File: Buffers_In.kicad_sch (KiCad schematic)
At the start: 31 parts, among them U4 NE5532, U5 NE5532, X1 PEDAL_COMBO_TOP

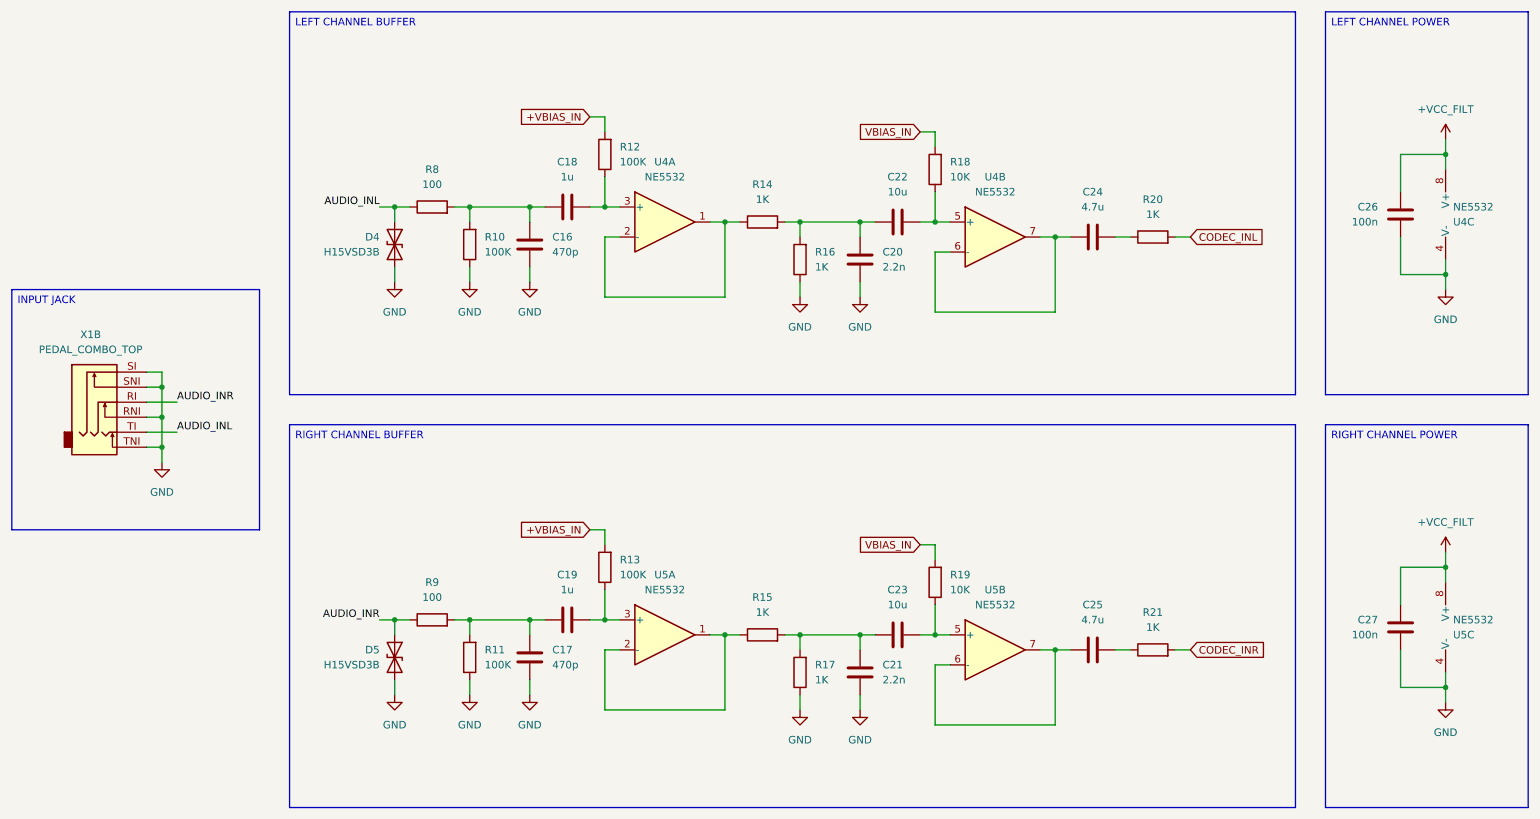
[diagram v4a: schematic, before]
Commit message: RP2350 layout
Updated the layout for the RP2350.
Added board headers.
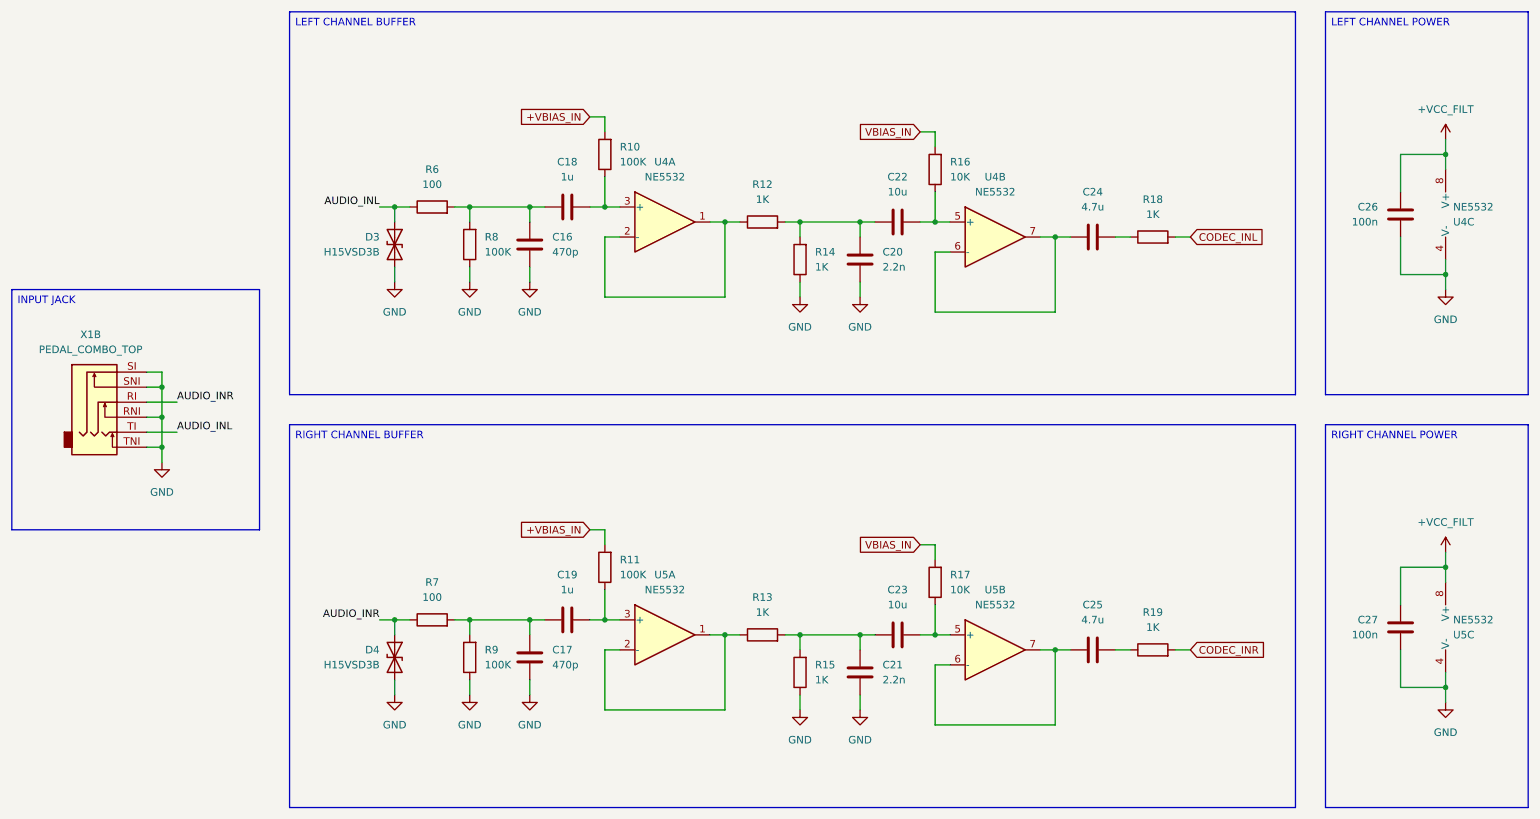
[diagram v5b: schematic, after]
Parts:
- renumbered D4 to D3, D5 to D4, R12 to R10, R13 to R11, R14 to R12, R15 to R13, R16 to R14, R17 to R15, R18 to R16, R19 to R17, R20 to R18, R21 to R19, R8 to R6, R9 to R7, R10 to R8, R11 to R9
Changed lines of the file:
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@@
 		(dnp no)
 		(fields_autoplaced yes)
-		(property "Reference" "R9"
+		(property "Reference" "R7"
 			(at 90.17 118.11 90)
 			(effects
@@
 			(project "SimpleCodec"
 				(path "/4cbf131b-42e8-4a05-beea-68c6d66cdb1a/469e8ad1-854f-4ea5-8b66-be90c8cb100f"
-					(reference "R9")
+					(reference "R7")
 					(unit 1)
 				)
@@
 		(dnp no)
 		(fields_autoplaced yes)
-		(property "Reference" "R19"
+		(property "Reference" "R17"
 			(at 177.8 116.8399 0)
 			(effects
@@
 			(project "SimpleCodec"
 				(path "/4cbf131b-42e8-4a05-beea-68c6d66cdb1a/469e8ad1-854f-4ea5-8b66-be90c8cb100f"
-					(reference "R19")
+					(reference "R17")
 					(unit 1)
 				)
@@
 		(dnp no)
 		(fields_autoplaced yes)
-		(property "Reference" "R18"
+		(property "Reference" "R16"
 			(at 177.8 46.9899 0)
 			(effects
@@
 			(project "SimpleCodec"
 				(path "/4cbf131b-42e8-4a05-beea-68c6d66cdb1a/469e8ad1-854f-4ea5-8b66-be90c8cb100f"
-					(reference "R18")
+					(reference "R16")
 					(unit 1)
 				)
@@
 		(dnp no)
 		(fields_autoplaced yes)
-		(property "Reference" "R21"
+		(property "Reference" "R19"
 			(at 212.09 123.19 90)
 			(effects
@@
 			(project "SimpleCodec"
 				(path "/4cbf131b-42e8-4a05-beea-68c6d66cdb1a/469e8ad1-854f-4ea5-8b66-be90c8cb100f"
-					(reference "R21")
+					(reference "R19")
 					(unit 1)
 				)
@@
 		(dnp no)
 		(fields_autoplaced yes)
-		(property "Reference" "R14"
+		(property "Reference" "R12"
 			(at 146.05 50.8 90)
 			(effects
@@
 			(project "SimpleCodec"
 				(path "/4cbf131b-42e8-4a05-beea-68c6d66cdb1a/469e8ad1-854f-4ea5-8b66-be90c8cb100f"
-					(reference "R14")
+					(reference "R12")
 					(unit 1)
 				)
@@
 		(dnp no)
 		(fields_autoplaced yes)
-		(property "Reference" "R10"
+		(property "Reference" "R8"
 			(at 99.06 59.6899 0)
 			(effects
@@
 			(project "SimpleCodec"
 				(path "/4cbf131b-42e8-4a05-beea-68c6d66cdb1a/469e8ad1-854f-4ea5-8b66-be90c8cb100f"
-					(reference "R10")
+					(reference "R8")
 					(unit 1)
 				)
@@
 		(dnp no)
 		(fields_autoplaced yes)
-		(property "Reference" "R16"
+		(property "Reference" "R14"
 			(at 154.94 62.2299 0)
 			(effects
@@
 			(project "SimpleCodec"
 				(path "/4cbf131b-42e8-4a05-beea-68c6d66cdb1a/469e8ad1-854f-4ea5-8b66-be90c8cb100f"
-					(reference "R16")
+					(reference "R14")
 					(unit 1)
 				)
@@
 		(dnp no)
 		(fields_autoplaced yes)
-		(property "Reference" "R12"
+		(property "Reference" "R10"
 			(at 121.92 44.4499 0)
 			(effects
@@
 			(project "SimpleCodec"
 				(path "/4cbf131b-42e8-4a05-beea-68c6d66cdb1a/469e8ad1-854f-4ea5-8b66-be90c8cb100f"
-					(reference "R12")
+					(reference "R10")
 					(unit 1)
 				)
@@
 		(dnp no)
 		(fields_autoplaced yes)
-		(property "Reference" "R17"
+		(property "Reference" "R15"
 			(at 154.94 132.0799 0)
 			(effects
@@
 			(project "SimpleCodec"
 				(path "/4cbf131b-42e8-4a05-beea-68c6d66cdb1a/469e8ad1-854f-4ea5-8b66-be90c8cb100f"
-					(reference "R17")
+					(reference "R15")
 					(unit 1)
 				)
@@
 		(dnp no)
 		(fields_autoplaced yes)
-		(property "Reference" "R20"
+		(property "Reference" "R18"
 			(at 212.09 53.34 90)
 			(effects
@@
 			(project "SimpleCodec"
 				(path "/4cbf131b-42e8-4a05-beea-68c6d66cdb1a/469e8ad1-854f-4ea5-8b66-be90c8cb100f"
-					(reference "R20")
+					(reference "R18")
 					(unit 1)
 				)
@@
 		(dnp no)
 		(fields_autoplaced yes)
-		(property "Reference" "R8"
+		(property "Reference" "R6"
 			(at 90.17 48.26 90)
 			(effects
@@
 			(project "SimpleCodec"
 				(path "/4cbf131b-42e8-4a05-beea-68c6d66cdb1a/469e8ad1-854f-4ea5-8b66-be90c8cb100f"
-					(reference "R8")
+					(reference "R6")
 					(unit 1)
 				)
@@
 		(dnp no)
 		(fields_autoplaced yes)
-		(property "Reference" "R11"
+		(property "Reference" "R9"
 			(at 99.06 129.5399 0)
 			(effects
@@
 			(project "SimpleCodec"
 				(path "/4cbf131b-42e8-4a05-beea-68c6d66cdb1a/469e8ad1-854f-4ea5-8b66-be90c8cb100f"
-					(reference "R11")
+					(reference "R9")
 					(unit 1)
 				)
@@
 		(dnp no)
 		(fields_autoplaced yes)
-		(property "Reference" "R15"
+		(property "Reference" "R13"
 			(at 146.05 120.65 90)
 			(effects
@@
 			(project "SimpleCodec"
 				(path "/4cbf131b-42e8-4a05-beea-68c6d66cdb1a/469e8ad1-854f-4ea5-8b66-be90c8cb100f"
-					(reference "R15")
+					(reference "R13")
 					(unit 1)
 				)
@@
 		(on_board yes)
 		(dnp no)
-		(property "Reference" "D4"
+		(property "Reference" "D3"
 			(at 81.28 59.6901 90)
 			(effects
@@
 			(project "SimpleCodec"
 				(path "/4cbf131b-42e8-4a05-beea-68c6d66cdb1a/469e8ad1-854f-4ea5-8b66-be90c8cb100f"
-					(reference "D4")
+					(reference "D3")
 					(unit 1)
 				)
@@
 		(on_board yes)
 		(dnp no)
-		(property "Reference" "D5"
+		(property "Reference" "D4"
 			(at 81.28 129.5401 90)
 			(effects
@@
 			(project "SimpleCodec"
 				(path "/4cbf131b-42e8-4a05-beea-68c6d66cdb1a/469e8ad1-854f-4ea5-8b66-be90c8cb100f"
-					(reference "D5")
+					(reference "D4")
 					(unit 1)
 				)
@@
 		(dnp no)
 		(fields_autoplaced yes)
-		(property "Reference" "R13"
+		(property "Reference" "R11"
 			(at 121.92 114.2999 0)
 			(effects
@@
 			(project "SimpleCodec"
 				(path "/4cbf131b-42e8-4a05-beea-68c6d66cdb1a/469e8ad1-854f-4ea5-8b66-be90c8cb100f"
-					(reference "R13")
-					(unit 1)
-				)
+					(reference "R11")
+					(unit 1)
+				)
